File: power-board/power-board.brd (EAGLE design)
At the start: 75 x 40 mm, 19 parts, among them J1 1X2-3.5MM, J2 1X2-3.5MM, J3 1X2-3.5MM, J4 1X2-3.5MM

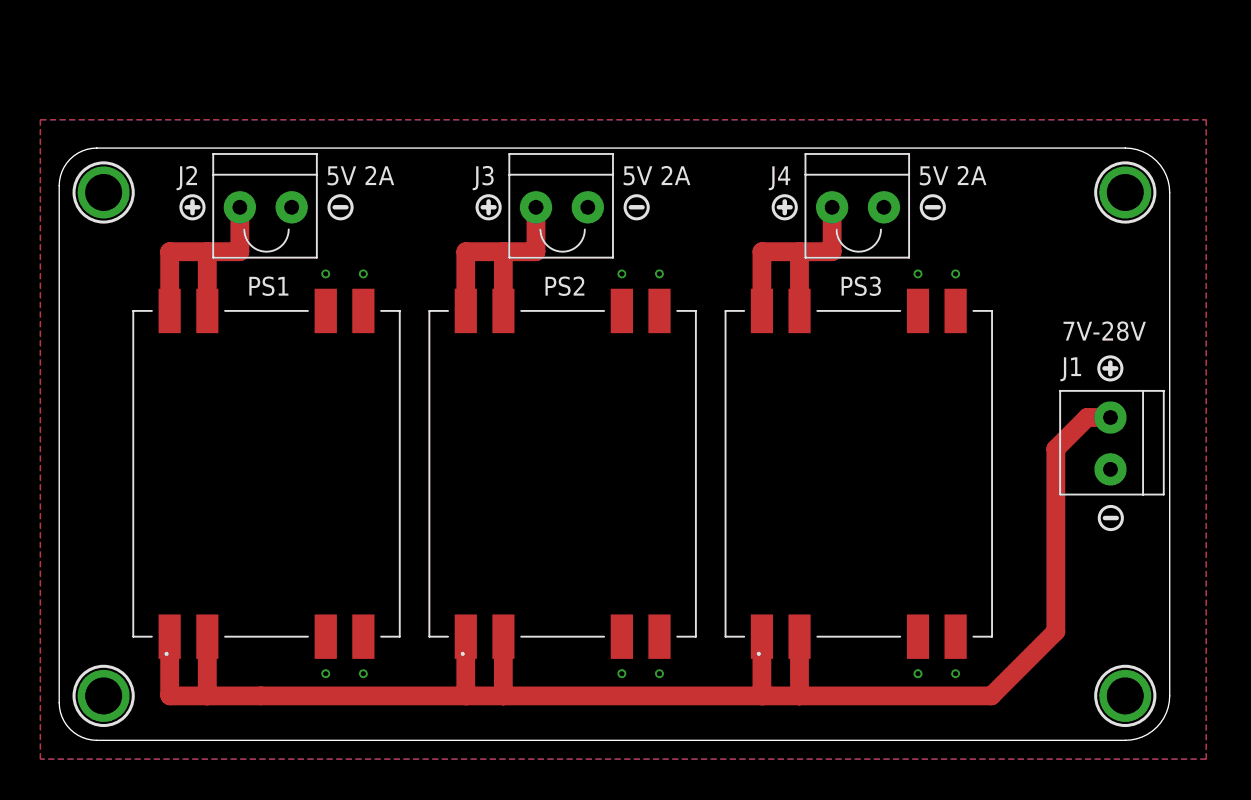
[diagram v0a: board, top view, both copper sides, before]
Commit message: Add Power-Hat
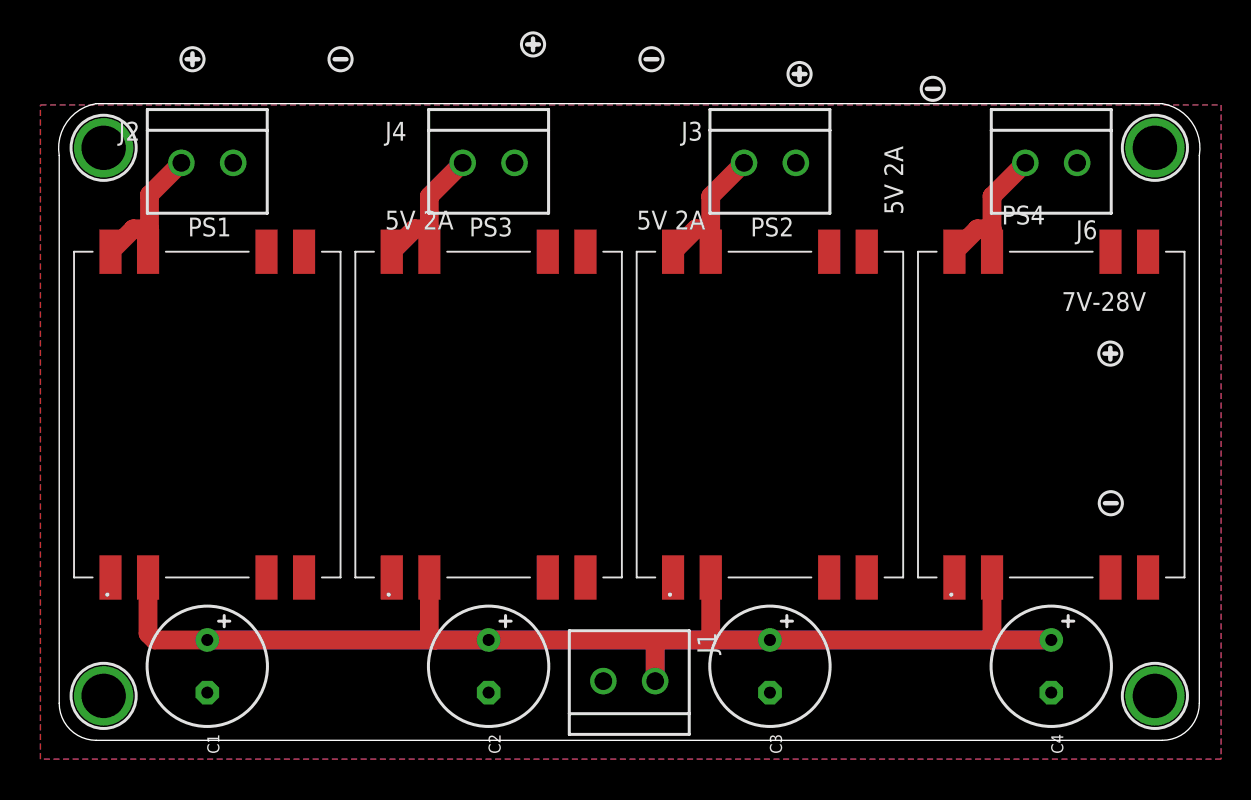
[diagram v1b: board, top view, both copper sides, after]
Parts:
- added C1, C2, C3, C4: (no value), sanisimov:CELEC_3.5MM_8MM
- added J6: (no value), sanisimov:WR-TBL-1X2-3.5MM
- added PS4: 5V, sanisimov:K8801
- J1, J2, J3, J4: value 1X2-3.5MM -> (none); device adafruit:1X2-3.5MM -> sanisimov:WR-TBL-1X2-3.5MM
- U$1, U$2, U$3, U$4: value MICROBUILDER_MOUNTINGHOLE2.5 -> MOUNTINGHOLE3.0THIN; device Adafruit DRV8871:MICROBUILDER_MOUNTINGHOLE_2.5_PLATED -> sanisimov:MOUNTINGHOLE_3.0_PLATEDTHIN
- moved J1 36.2 mm to (38.5, 4.00), turned to 0 degrees
- moved PS3 25.3 mm to (29.0, 22.0)
- moved J4 25.2 mm to (29.0, 39.0)
- moved PS2 14.6 mm to (48.0, 22.0)
- moved J3 14.3 mm to (48.0, 39.0)
- moved U$11 11.4 mm to (32.0, 47.0)
- moved U$12 10.0 mm to (40.0, 46.0)
- moved U$5 10.0 mm to (9.00, 46.0)
- moved U$6 10.0 mm to (19.0, 46.0)
- moved U$7 9.06 mm to (50.0, 45.0)
- moved U$8 8.00 mm to (59.0, 44.0)
- moved PS1 5.66 mm to (10.0, 22.0)
- moved J2 5.00 mm to (10.0, 39.0)
- moved U$4 3.62 mm to (74.0, 40.0)
- moved U$1 3.02 mm to (3.00, 40.0)
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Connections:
- new net N$1: J6.1, PS4.5, PS4.6
- net GND: now also C1.-, C2.-, C3.-, C4.-, J6.2, PS4.3, PS4.4, PS4.7, PS4.8
- net VCC: now also C1.+, C2.+, C3.+, C4.+, PS4.1, PS4.2
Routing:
- net VCC: track 102.6 -> 140.8 mm
- net N$1: track 0.00 -> 10.1 mm
- net N$5: track 15.7 -> 10.1 mm
- net N$3: track 15.7 -> 10.1 mm
- net N$7: track 15.7 -> 10.2 mm
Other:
- board size 75 x 40 mm -> 77.1 x 43 mm
- board text removed: "?"

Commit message: Publish v1.0.0 Power Board and Power Bridge
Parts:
- removed C2, C3, C4: (no value), sanisimov:CELEC_3.5MM_8MM
- removed J1, J2, J3, J4, J6: (no value), sanisimov:WR-TBL-1X2-3.5MM
- removed PS2, PS3, PS4: 5V, sanisimov:K8801
- removed U$1, U$4: MOUNTINGHOLE3.0THIN, sanisimov:MOUNTINGHOLE_3.0_PLATEDTHIN
- removed U$10, U$12, U$6, U$8: (no value), microbuilder:SYMBOL_MINUS
- removed U$11, U$5, U$7, U$9: (no value), microbuilder:SYMBOL_PLUS
- added X1: CON-FE02-1, _Library.b1f76137-4d0f-4ce2-9703-0cd83550450f.flbr:PTSM0,5/2-2,5-HTHRR24
- added X2: CON-FE02-2HDRVR4W64P254_2X2, _Library.b1f76137-4d0f-4ce2-9703-0cd83550450f.flbr:HDRVR4W64P254_2X2
- added X3, X4: CON-MA02-1, _Library.b1f76137-4d0f-4ce2-9703-0cd83550450f.flbr:AVX-BTB-009159002001106
- C1: value (none) -> CAP_ELECTROLYTIC; device sanisimov:CELEC_3.5MM_8MM -> _Library.b1f76137-4d0f-4ce2-9703-0cd83550450f.flbr:CAPPRD350W60D800H800B
- PS1: value 5V -> (none); device sanisimov:K8801 -> _Library.b1f76137-4d0f-4ce2-9703-0cd83550450f.flbr:K8801
- U$2, U$3: value MOUNTINGHOLE3.0THIN -> MOUNTINGHOLE2.7_THICK; device sanisimov:MOUNTINGHOLE_3.0_PLATEDTHIN -> _Library.b1f76137-4d0f-4ce2-9703-0cd83550450f.flbr:MOUNTINGHOLE_2.7_PLATED_THICK
- moved U$3 78.4 mm to (6.00, 42.0)
- moved U$2 19.5 mm to (21.0, 10.5)
- moved C1 7.43 mm to (5.00, 10.5), turned to 180 degrees
- moved PS1 4.03 mm to (13.5, 24.0), turned to 270 degrees
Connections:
- removed net N$3: J3.1, PS2.5, PS2.6
- removed net N$5: J4.1, PS3.5, PS3.6
- removed net N$7: J2.1, PS1.5, PS1.6
- removed net VCC: C1.+, C2.+, C3.+, C4.+, J1.1, PS1.1, PS1.2, PS2.1, PS2.2, PS3.1, PS3.2, PS4.1, PS4.2
- new net VIN: C1.1, PS1.1, PS1.2, X1.1, X1.2, X3.1, X3.3, X4.2, X4.4
- net GND: now also C1.2, X1.3, X1.4, X2.1, X2.2, X3.2, X3.4, X4.1, X4.3; no longer C1.-, C2.-, C3.-, C4.-, J1.2, J2.2, J3.2, J4.2, J6.2, PS2.3, PS2.4, PS2.7, PS2.8, PS3.3, PS3.4, PS3.7, PS3.8, PS4.3, PS4.4, PS4.7, PS4.8
- net N$1: now also PS1.5, PS1.6, X2.3, X2.4; no longer J6.1, PS4.5, PS4.6
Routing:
- net VCC: track 140.8 -> 0.00 mm
- net VIN: track 0.00 -> 132.5 mm, vias 0 -> 4
- net GND: track 0.00 -> 67.6 mm, vias 0 -> 8
- net N$1: track 10.1 -> 40.4 mm
- net N$7: track 10.2 -> 0.00 mm
- net N$3: track 10.1 -> 0.00 mm
- net N$5: track 10.1 -> 0.00 mm
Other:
- board size 77.1 x 43 mm -> 27 x 46 mm
- board text added: "7V-28V 5V 3A"
- board text removed: "5V 2A"
- board text removed: "7V-28V"
